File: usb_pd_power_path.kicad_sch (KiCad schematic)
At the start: 79 parts, among them Q10 Q_Dual_PMOS, Q11 Q_NMOS_DGS, Q12 Q_NMOS_DGS, Q13 Q_NMOS_DGS, Q14 Q_NMOS_DGS, Q15 Q_NMOS_DGS, Q16 Q_NMOS_DGS, Q9 Q_Dual_PMOS, U17 LM358, U18 MP2229GQ-P, U19 MP2229GQ-P

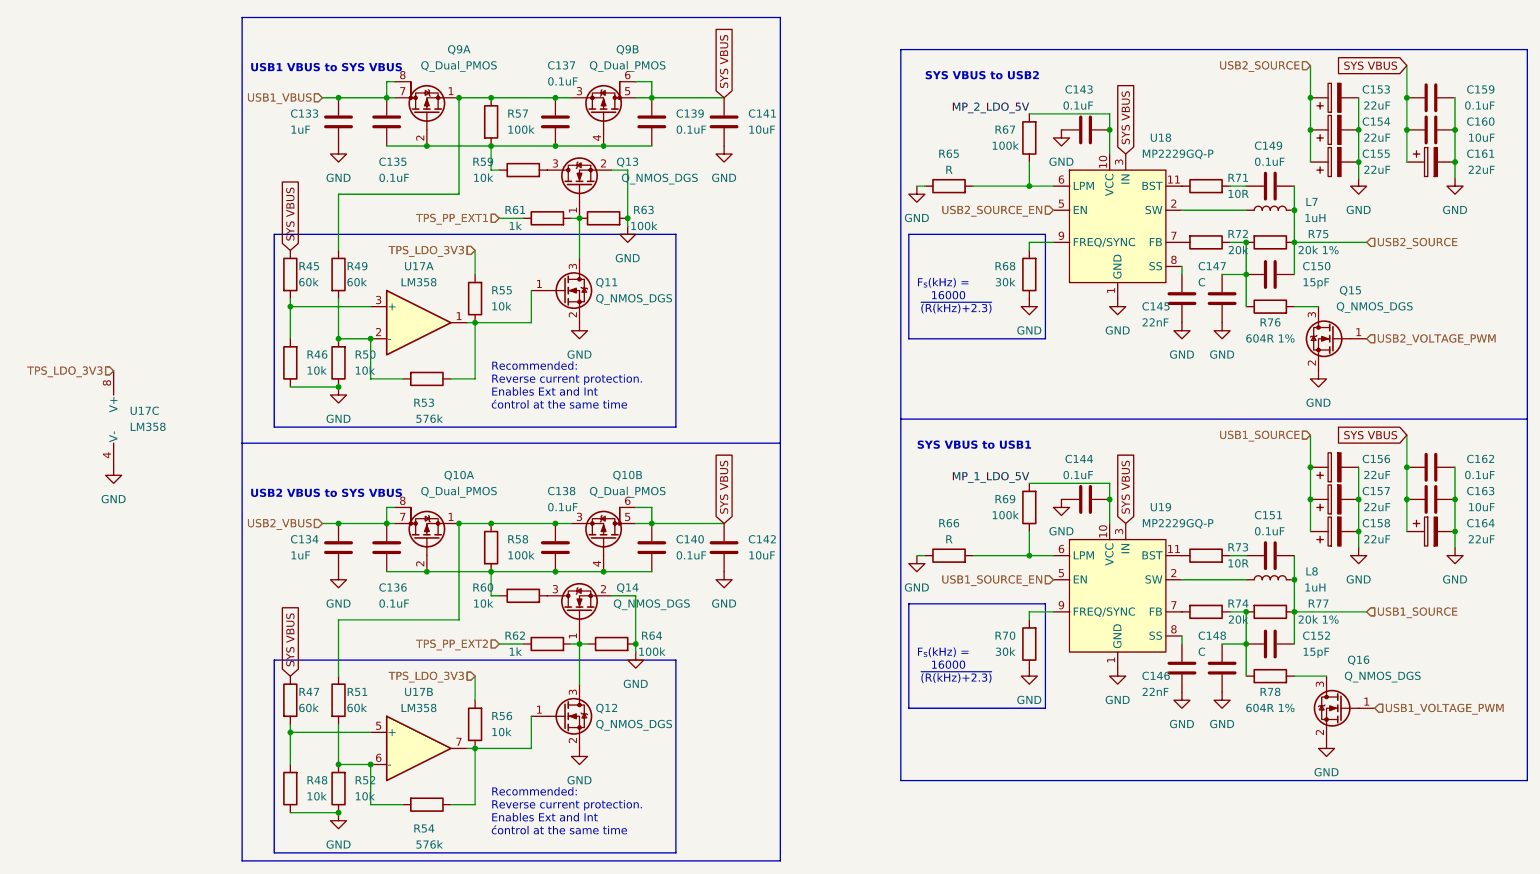
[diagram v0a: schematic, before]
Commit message: done first iteration of pcb routing, slikscreen still broken
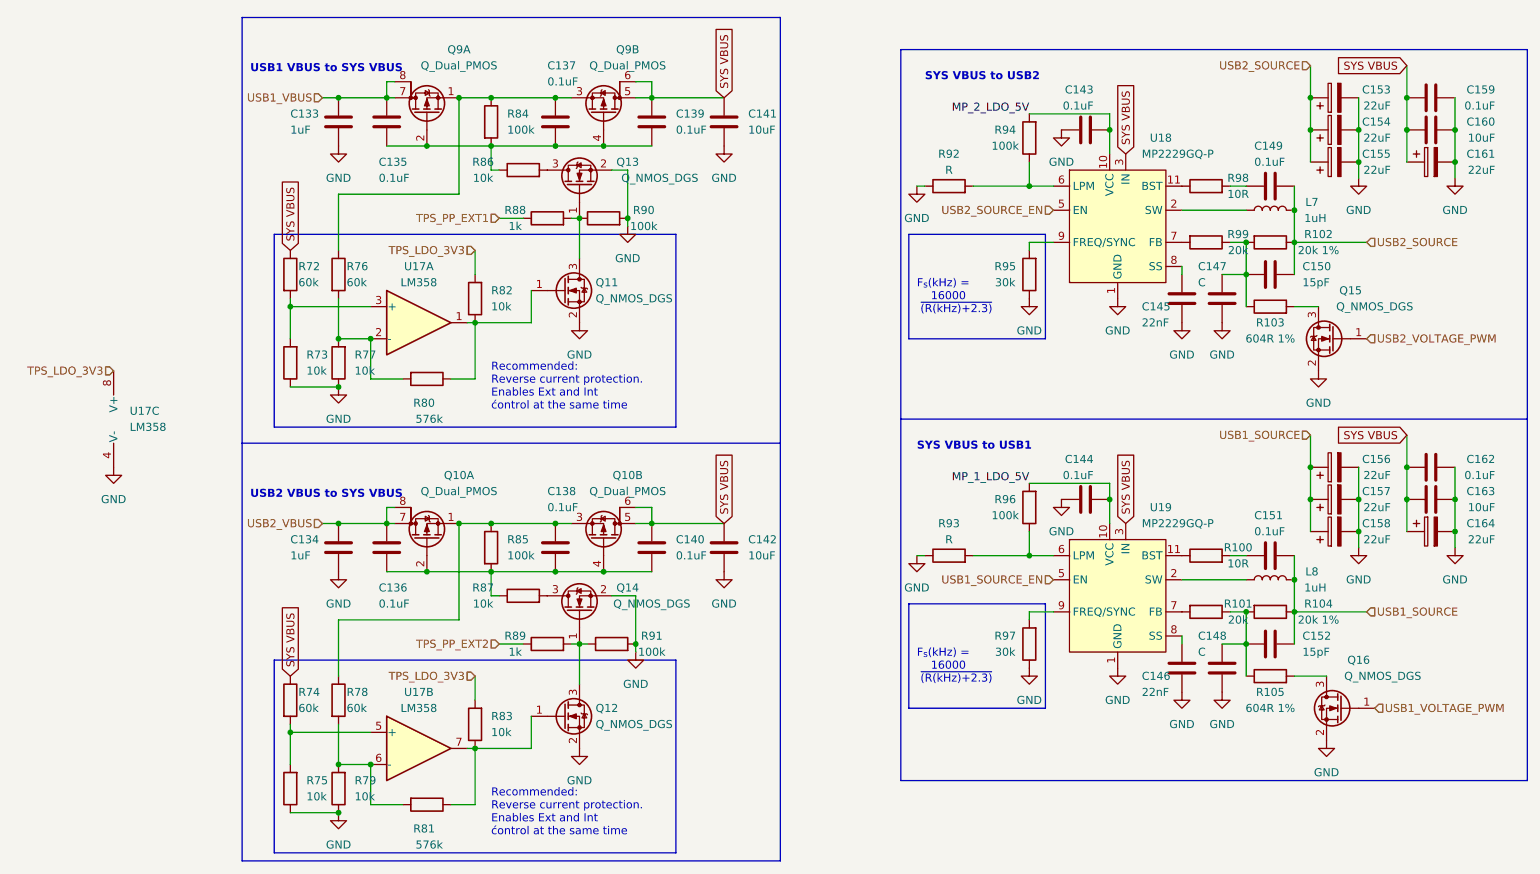
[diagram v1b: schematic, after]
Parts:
- renumbered R73 to R100, R74 to R101, R75 to R102, R76 to R103, R77 to R104, R78 to R105, R45 to R72, R46 to R73, R47 to R74, R48 to R75, R49 to R76, R50 to R77, R51 to R78, R52 to R79, R53 to R80, R54 to R81, R55 to R82, R56 to R83, R57 to R84, R58 to R85, R59 to R86, R60 to R87, R61 to R88, R62 to R89, R63 to R90, R64 to R91, R65 to R92, R66 to R93, R67 to R94, R68 to R95, R69 to R96, R70 to R97, R71 to R98, R72 to R99

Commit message: mounting holes, fixes silkscreen
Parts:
- renumbered C133 to C131, C134 to C132, C135 to C133, C136 to C134, C137 to C135, C138 to C136, C139 to C137, C140 to C138, C141 to C139, C142 to C140, C143 to C141, C144 to C142, C145 to C143, C146 to C144, C147 to C145, C148 to C146, C149 to C147, C150 to C148, C151 to C149, C152 to C150, C153 to C151, C154 to C152, C155 to C153, C156 to C154, C157 to C155, C158 to C156, C159 to C157, C160 to C158, C161 to C159, C162 to C160, C163 to C161, C164 to C162, R101 to R100, R102 to R101, R103 to R102, R104 to R103, R105 to R104, R72 to R71, R73 to R72, R74 to R73, R75 to R74, R76 to R75, R77 to R76, R78 to R77, R79 to R78, R80 to R79, R81 to R80, R82 to R81, R83 to R82, R84 to R83, R85 to R84, R86 to R85, R87 to R86, R88 to R87, R89 to R88, R90 to R89, R91 to R90, R92 to R91, R93 to R92, R94 to R93, R95 to R94, R96 to R95, R97 to R96, R98 to R97, R99 to R98, R100 to R99

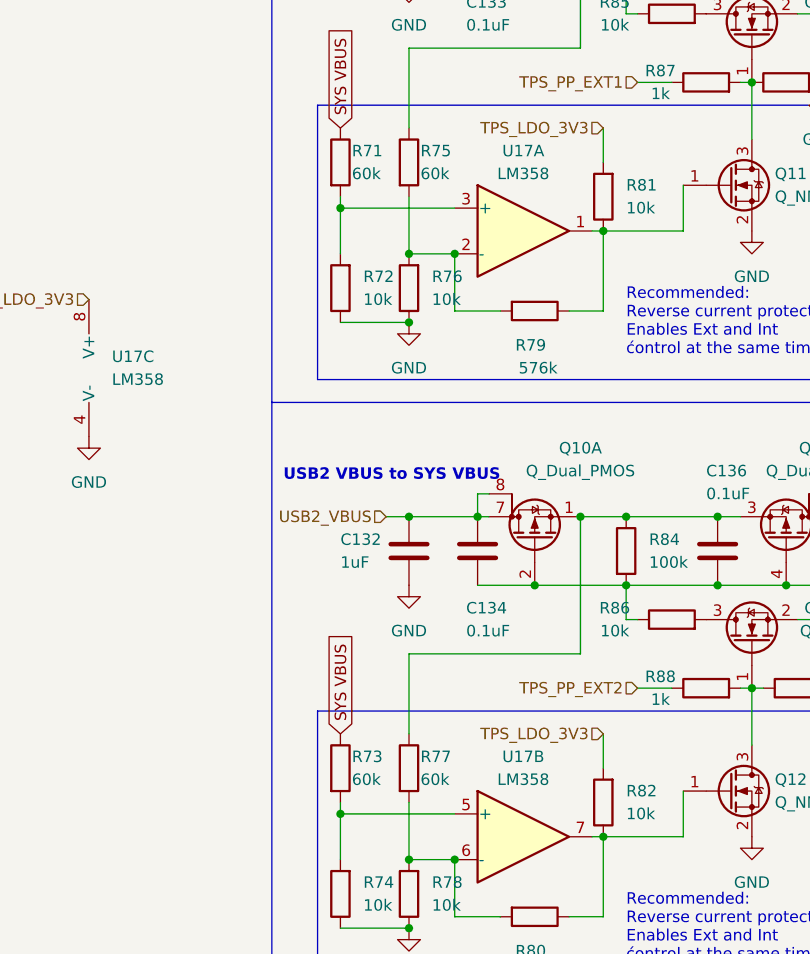
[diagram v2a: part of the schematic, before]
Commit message: minor setting changes in schematics, added test software container
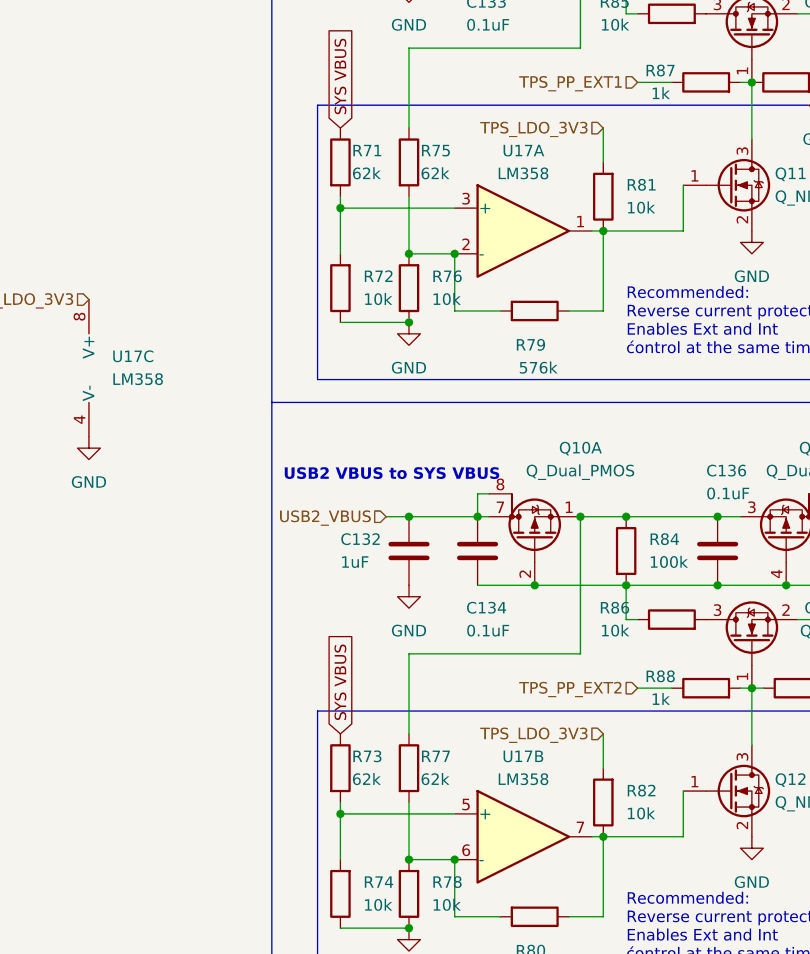
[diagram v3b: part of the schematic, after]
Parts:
- R71, R73, R75, R77: value 60k -> 62k
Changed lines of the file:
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@@
       (effects (font (size 1.27 1.27)) (justify left))
     )
-    (property "Value" "60k" (id 1) (at 78.74 66.04 0)
+    (property "Value" "62k" (id 1) (at 78.74 66.04 0)
       (effects (font (size 1.27 1.27)) (justify left))
     )
@@
       (effects (font (size 1.27 1.27)) (justify left))
     )
-    (property "Value" "60k" (id 1) (at 86.36 133.35 0)
+    (property "Value" "62k" (id 1) (at 86.36 133.35 0)
       (effects (font (size 1.27 1.27)) (justify left))
     )
@@
       (effects (font (size 1.27 1.27)) (justify left))
     )
-    (property "Value" "60k" (id 1) (at 78.74 133.35 0)
+    (property "Value" "62k" (id 1) (at 78.74 133.35 0)
       (effects (font (size 1.27 1.27)) (justify left))
     )
@@
       (effects (font (size 1.27 1.27)) (justify left))
     )
-    (property "Value" "60k" (id 1) (at 86.36 66.04 0)
-      (effects (font (size 1.27 1.27)) (justify left))
-    )
+    (property "Value" "62k" (id 1) (at 86.36 66.04 0)
+      (effects (font (size 1.27 1.27)) (justify left))
+    )
